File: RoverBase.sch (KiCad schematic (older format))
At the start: 64 parts, among them J1 Conn_01x01, J2 Conn_01x06, J3 Conn_01x04, J4 Conn_01x02, J5 Conn_01x03, J6 Conn_02x03_Counter_Clockwise, J7 Conn_02x03_Counter_Clockwise, J8 Conn_01x01, J9 Conn_01x06, SW1 SW_SPDT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

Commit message: Update board pins
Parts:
- BT1: Manufacturer (none) -> MPD (Memory Protection Devices)
- C1: Manufacturer (none) -> Yageo
- C10, C11, C14, C15: Manufacturer (none) -> TDK Corporation
- C12, C13, C2, C4, C5, C6, C7: Manufacturer (none) -> Murata Electronics
- C16: Manufacturer (none) -> Nichicon
- C17, C18: Manufacturer (none) -> Panasonic Electronic Components
- C19, C20, C3, C8, C9: Manufacturer (none) -> KEMET
- D1, D2, D3: Manufacturer (none) -> Lite-On Inc.
- D4, D5: Manufacturer (none) -> Infineon Technologies
- J1, J8, J9: MPN (none) -> nf; Manufacturer (none) -> nf; SPN (none) -> nf; fit_field (none) -> dnf
- J2: MPN (none) -> BM06B-GHS-TBT(LF)(SN)(N); Manufacturer (none) -> JST Sales America Inc.; SPN (none) -> 455-1582-1-ND
- J3: MPN nf -> 61300411121; Manufacturer (none) -> Würth Elektronik; SPN nf -> 732-5317-ND; fit_field dnf -> (none)
- J4, J5: Manufacturer (none) -> nf
- J6, J7: Manufacturer (none) -> Sullins Connector Solutions
- L1, L2, R1, R10, R11, R12, R13, R14, R2, R3, R4, R5, R6, R8, R9: Manufacturer (none) -> Vishay Dale
- SW1, SW2, SW3: Manufacturer (none) -> C&K
- U1: Manufacturer (none) -> STMicroelectronics
- U2: Manufacturer (none) -> Allegro MicroSystems
- U3, U4, U5, U6, U7: Manufacturer (none) -> Texas Instruments

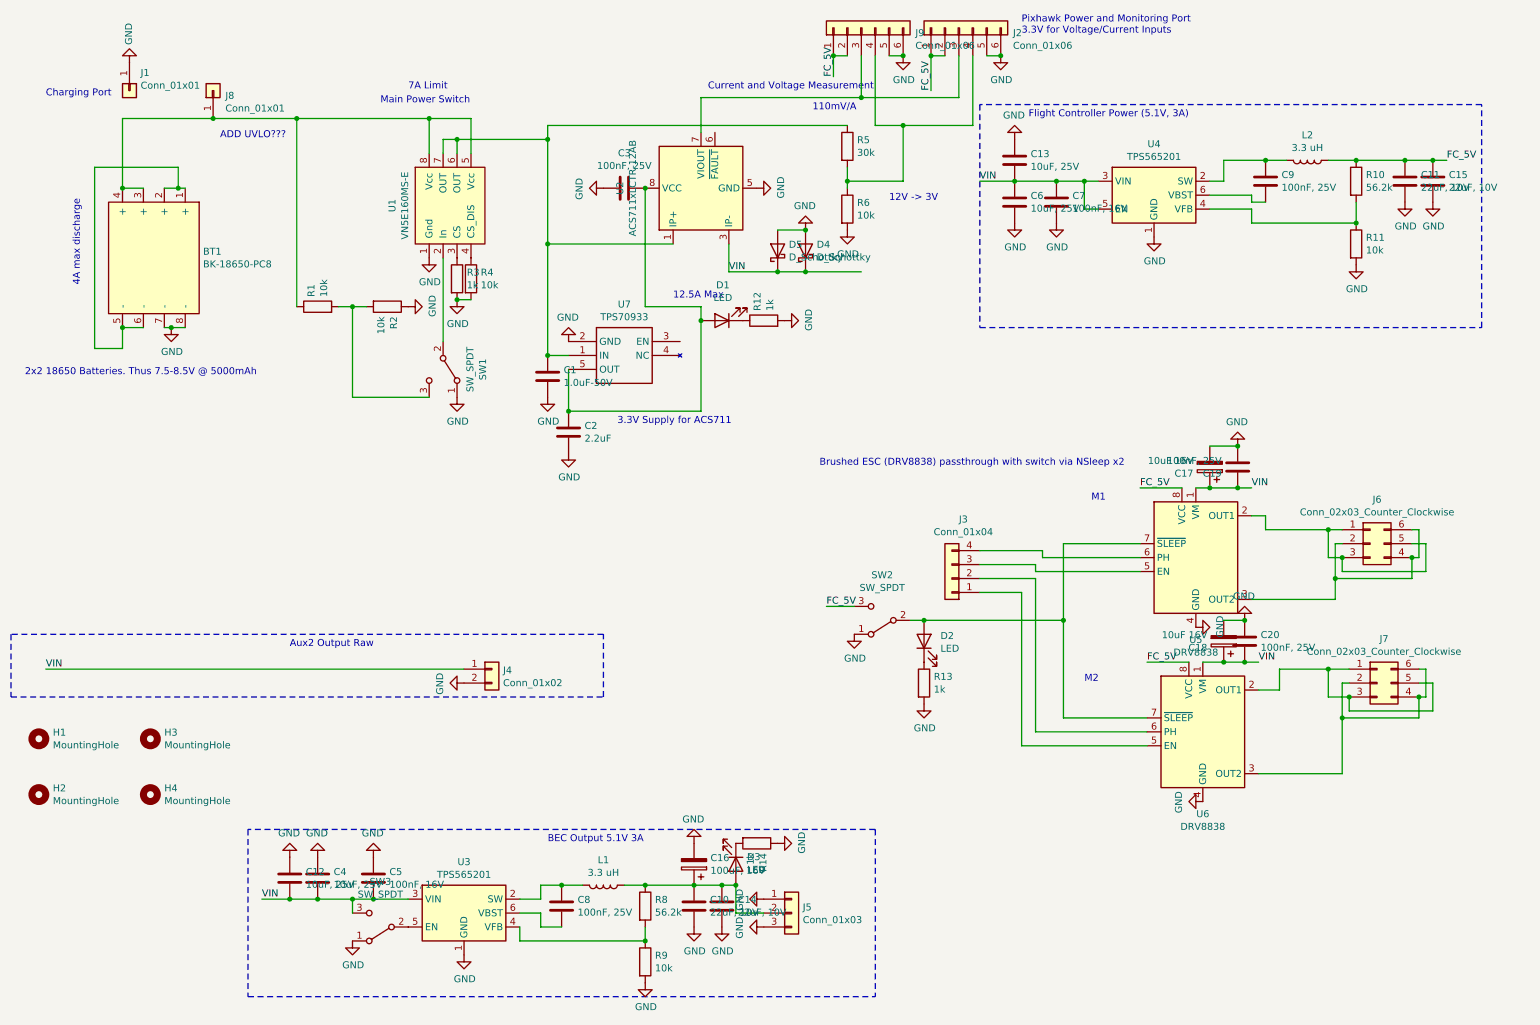
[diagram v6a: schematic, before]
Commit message: FC Power 5.1V to 5.3V
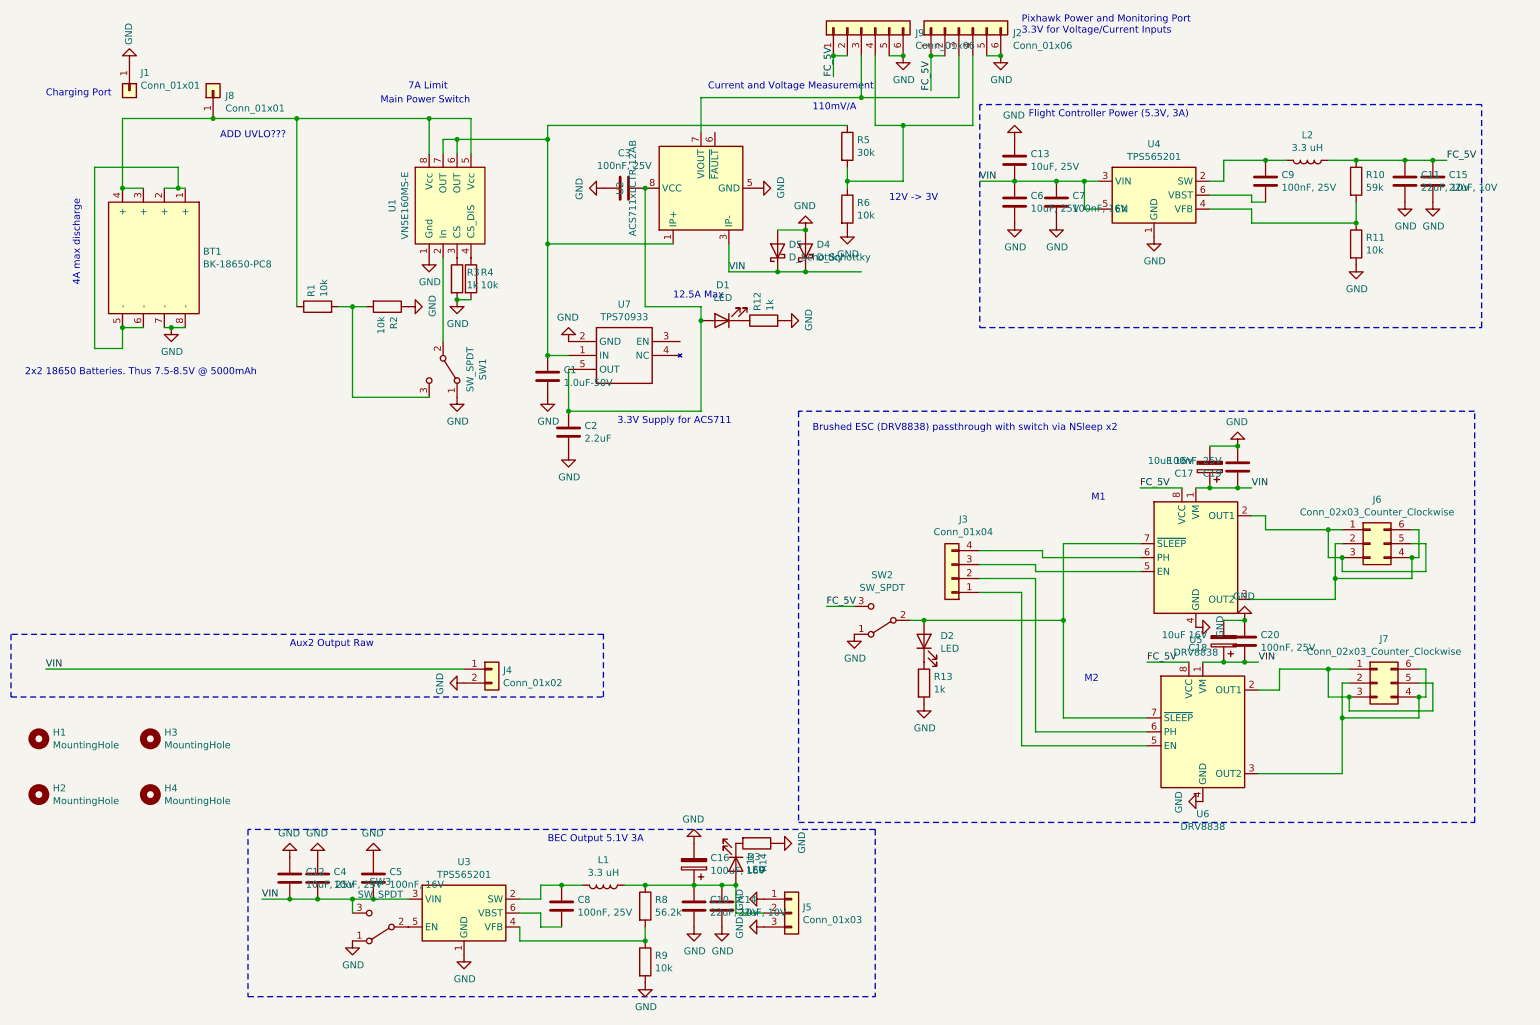
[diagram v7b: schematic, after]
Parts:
- R10: value 56.2k -> 59k; MPN CRCW040256K2FKED -> CRCW040259K0FKED; SPN 541-5017-1-ND -> 541-59.0KLCT-ND
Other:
- note added: "Flight Controller Power (5.3V, 3A)"
- note removed: "Flight Controller Power (5.1V, 3A)"
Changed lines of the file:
@@
 	5600 1400 5600 1150
 Text Notes 7950 1300 0    50   ~ 0
-Flight Controller Power (5.1V, 3A)
+Flight Controller Power (5.3V, 3A)
 Wire Wire Line
 	5800 2400 6150 2400
@@
 	1    0    0    -1
 $EndComp
-Text Notes 6450 3800 0    50   ~ 0
+Text Notes 6400 3550 0    50   ~ 0
 Brushed ESC (DRV8838) passthrough with switch via NSleep x2
 Text Notes 4500 6500 0    50   ~ 0
@@
 P 10300 1750
 F 0 "R10" H 10370 1796 50  0000 L CNN
-F 1 "56.2k" H 10370 1705 50  0000 L CNN
+F 1 "59k" H 10370 1705 50  0000 L CNN
 F 2 "Resistor_SMD:R_0402_1005Metric_Pad0.72x0.64mm_HandSolder" V 10230 1750 50  0001 C CNN
 F 3 "~" H 10300 1750 50  0001 C CNN
-F 4 "CRCW040256K2FKED" H 10300 1750 50  0001 C CNN "MPN"
-F 5 "541-5017-1-ND" H 10300 1750 50  0001 C CNN "SPN"
+F 4 "CRCW040259K0FKED" H 10300 1750 50  0001 C CNN "MPN"
+F 5 "541-59.0KLCT-ND" H 10300 1750 50  0001 C CNN "SPN"
 F 6 "Vishay Dale" H 10300 1750 50  0001 C CNN "Manufacturer"
 	1    10300 1750
@@
 Text Label 6550 1000 1    50   ~ 0
 FC_5V
+Wire Notes Line
+	6300 3400 6300 6350
+Wire Notes Line
+	6300 6350 11150 6350
+Wire Notes Line
+	11150 6350 11150 3400
+Wire Notes Line
+	11150 3400 6300 3400
 $EndSCHEMATC

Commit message: Cleanup and consolidate
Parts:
- C1: value 1.0uF-50V -> 1.0uF, 50V
- C19, C20, C3: value 100nF, 25V -> 100nF, 16V; footprint Capacitor_SMD:C_0603_1608Metric -> Capacitor_SMD:C_0402_1005Metric; MPN C0603C104Z3VACTU -> GRM155R71C104KA88D; Manufacturer KEMET -> Murata Electronics; SPN 399-1100-1-ND -> 490-3261-1-ND
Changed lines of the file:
@@
 encoding utf-8
 Sheet 1 1
-Title "Bogie Runt Rover Power and Motor Board"
+Title "RoverBase"
 Date ""
-Rev ""
-Comp ""
+Rev "1.1"
+Comp "Rpanion Electronics"
 Comment1 ""
 Comment2 ""
@@
 P 4500 3150
 F 0 "C1" H 4615 3196 50  0000 L CNN
-F 1 "1.0uF-50V" H 4615 3105 50  0000 L CNN
+F 1 "1.0uF, 50V" H 4615 3105 50  0000 L CNN
 F 2 "Capacitor_SMD:C_0805_2012Metric" H 4538 3000 50  0001 C CNN
 F 3 "~" H 4500 3150 50  0001 C CNN
@@
 P 5050 1800
 F 0 "C3" V 4798 1800 50  0000 C CNN
-F 1 "100nF, 25V" V 4889 1800 50  0000 C CNN
-F 2 "Capacitor_SMD:C_0603_1608Metric" H 5088 1650 50  0001 C CNN
+F 1 "100nF, 16V" V 4889 1800 50  0000 C CNN
+F 2 "Capacitor_SMD:C_0402_1005Metric" H 5088 1650 50  0001 C CNN
 F 3 "~" H 5050 1800 50  0001 C CNN
-F 4 "C0603C104Z3VACTU" H 5050 1800 50  0001 C CNN "MPN"
-F 5 "399-1100-1-ND" H 5050 1800 50  0001 C CNN "SPN"
-F 6 "KEMET" H 5050 1800 50  0001 C CNN "Manufacturer"
+F 4 "GRM155R71C104KA88D" H 5050 1800 50  0001 C CNN "MPN"
+F 5 "490-3261-1-ND" H 5050 1800 50  0001 C CNN "SPN"
+F 6 "Murata Electronics" H 5050 1800 50  0001 C CNN "Manufacturer"
 	1    5050 1800
 	0    1    1    0
@@
 P 9450 3800
 F 0 "C19" H 9565 3846 50  0000 L CNN
-F 1 "100nF, 25V" H 9565 3755 50  0000 L CNN
-F 2 "Capacitor_SMD:C_0603_1608Metric" H 9488 3650 50  0001 C CNN
+F 1 "100nF, 16V" H 9565 3755 50  0000 L CNN
+F 2 "Capacitor_SMD:C_0402_1005Metric" H 9488 3650 50  0001 C CNN
 F 3 "~" H 9450 3800 50  0001 C CNN
-F 4 "C0603C104Z3VACTU" H 9450 3800 50  0001 C CNN "MPN"
-F 5 "399-1100-1-ND" H 9450 3800 50  0001 C CNN "SPN"
-F 6 "KEMET" H 9450 3800 50  0001 C CNN "Manufacturer"
+F 4 "GRM155R71C104KA88D" H 9450 3800 50  0001 C CNN "MPN"
+F 5 "490-3261-1-ND" H 9450 3800 50  0001 C CNN "SPN"
+F 6 "Murata Electronics" H 9450 3800 50  0001 C CNN "Manufacturer"
 	1    9450 3800
 	-1   0    0    1
@@
 P 9500 5050
 F 0 "C20" H 9615 5096 50  0000 L CNN
-F 1 "100nF, 25V" H 9615 5005 50  0000 L CNN
-F 2 "Capacitor_SMD:C_0603_1608Metric" H 9538 4900 50  0001 C CNN
+F 1 "100nF, 16V" H 9615 5005 50  0000 L CNN
+F 2 "Capacitor_SMD:C_0402_1005Metric" H 9538 4900 50  0001 C CNN
 F 3 "~" H 9500 5050 50  0001 C CNN
-F 4 "C0603C104Z3VACTU" H 9500 5050 50  0001 C CNN "MPN"
-F 5 "399-1100-1-ND" H 9500 5050 50  0001 C CNN "SPN"
-F 6 "KEMET" H 9500 5050 50  0001 C CNN "Manufacturer"
+F 4 "GRM155R71C104KA88D" H 9500 5050 50  0001 C CNN "MPN"
+F 5 "490-3261-1-ND" H 9500 5050 50  0001 C CNN "SPN"
+F 6 "Murata Electronics" H 9500 5050 50  0001 C CNN "Manufacturer"
 	1    9500 5050
 	1    0    0    -1
